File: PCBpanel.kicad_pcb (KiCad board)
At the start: 2 copper layers, 29 x 40 mm, 87 parts, among them P1 CONN_01X05, P1 CONN_01X13, P1 CONN_buzz, P2 CONN_01X03, P2 CONN_01X09, P3 CONN_01X04, P3 CONN_01X09, P3 CONN_01X13, P4 CONN_01X02, Q1 BSS138, Q1 BSS84, Q1 NPN, Q2 BSS138, SW1 SW_PUSH, U1 ESP-12E, U1 GY-NEO6MV2, U2 AP1117, U3 ESP8266_THING, U4 MPU6050, U5 NVSRAM, U6 BMP180, U7 HTU21D

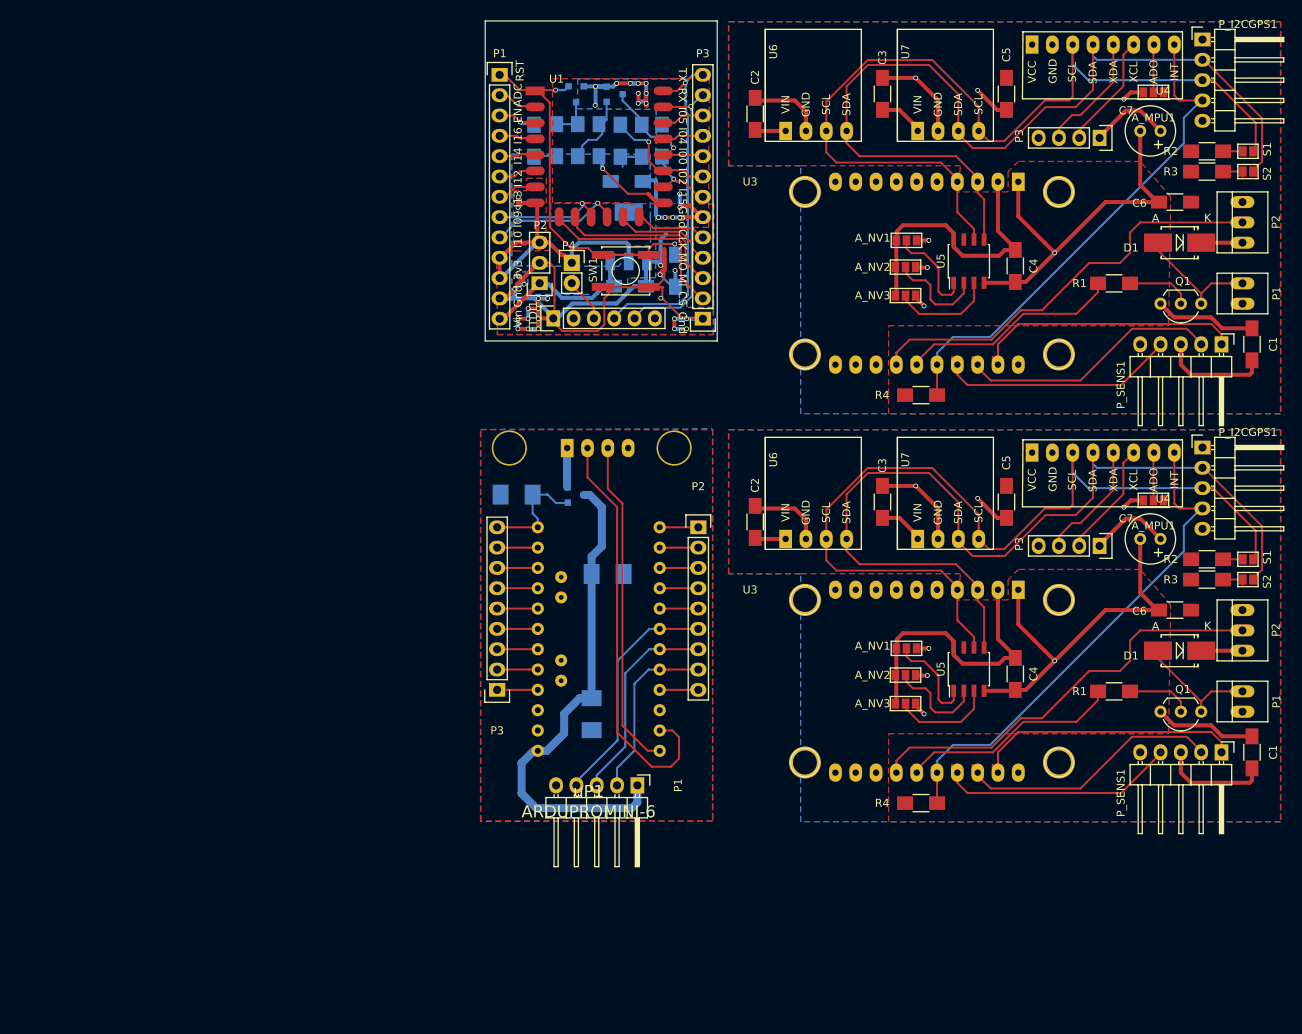
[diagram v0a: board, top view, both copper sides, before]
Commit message: added mounting hole and fixed footprint error
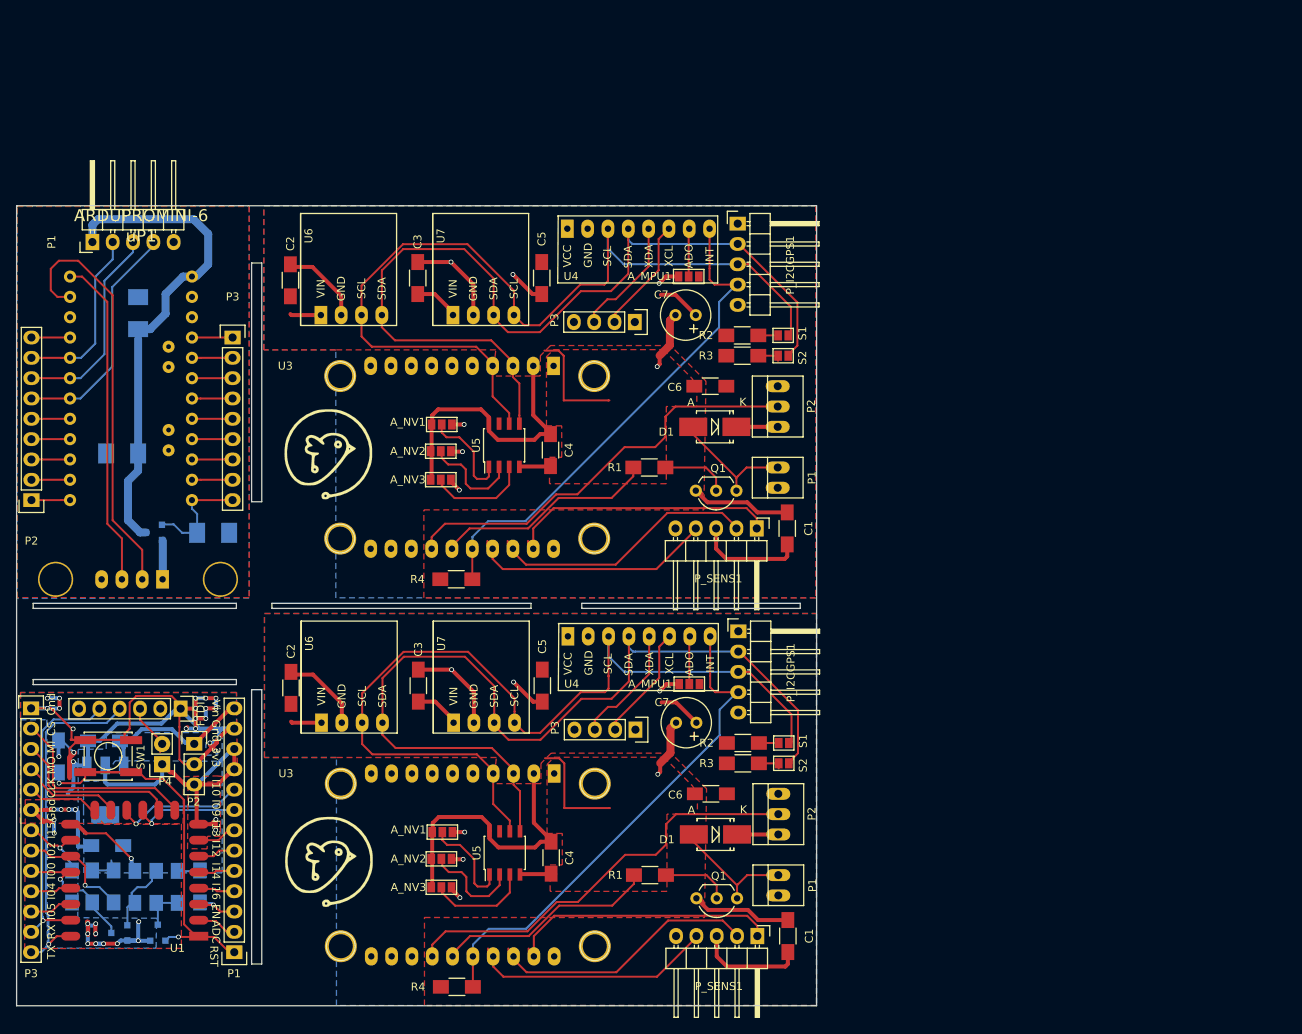
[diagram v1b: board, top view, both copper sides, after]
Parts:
- removed the A_MPU1 at (192.1, 35.8)
- removed the A_MPU1 at (192.1, 86.8)
- removed the A_NV1 at (161.2, 54.3)
- removed the A_NV1 at (161.2, 105.3)
- removed the A_NV2 at (161.1, 57.7)
- removed the A_NV2 at (161.1, 108.7)
- removed the A_NV3 at (161.1, 61.2)
- removed the A_NV3 at (161.1, 112.2)
- removed the C1 at (204.4, 67.3)
- removed the C1 at (204.4, 118.3)
- removed the C2 at (142.3, 38.5)
- removed the C2 at (142.3, 89.5)
- removed the C3 at (158.2, 36.0)
- removed the C3 at (158.2, 87.0)
- removed the C4 at (174.8, 57.5)
- removed the C4 at (174.8, 108.5)
- removed the C5 at (173.7, 36.0)
- removed the C5 at (173.7, 87.0)
- removed the C6 at (194.8, 49.5)
- removed the C6 at (194.8, 100.5)
- removed the C7 at (193.0, 40.6)
- removed the C7 at (193.0, 91.7)
- removed the D1 at (195.4, 54.6)
- removed the D1 at (195.4, 105.6)
- removed the P1 at (203.2, 61.0)
- removed the P1 at (203.2, 112.0)
- removed the P2 at (203.2, 52.1)
- removed the P2 at (203.2, 103.1)
- removed the P3 at (185.4, 41.5)
- removed the P3 at (185.4, 92.5)
- removed the P_I2CGPS1 at (198.2, 29.2)
- removed the P_I2CGPS1 at (198.2, 80.2)
- removed the P_SENS1 at (200.6, 67.3)
- removed the P_SENS1 at (200.6, 118.3)
- removed the Q1 at (198.1, 62.2)
- removed the Q1 at (198.1, 113.2)
- removed the R1 at (187.2, 59.7)
- removed the R1 at (187.2, 110.7)
- removed the R2 at (198.8, 43.2)
- removed the R2 at (198.8, 94.2)
- removed the R3 at (198.8, 45.7)
- removed the R3 at (198.8, 96.7)
- removed the R4 at (163.1, 73.7)
- removed the R4 at (163.1, 124.7)
- removed the S1 at (203.9, 43.2)
- removed the S1 at (203.9, 94.2)
- removed the S2 at (203.9, 45.7)
- removed the S2 at (203.9, 96.7)
- removed the U3 at (191.7, 45.7)
- removed the U3 at (191.7, 96.7)
- removed the U4 at (195.7, 31.6)
- removed the U4 at (195.7, 82.6)
- removed the U5 at (169.0, 56.9)
- removed the U5 at (169.0, 107.9)
- removed the U6 at (143.6, 41.9)
- removed the U6 at (143.6, 92.9)
- removed the U7 at (160.1, 41.9)
- removed the U7 at (160.1, 92.9)
- added A_MPU1: GS_A0, Connect:GS3, F.Cu at (134.0, 58.8)
- added A_MPU1: GS_A0, Connect:GS3, F.Cu at (134.1, 109.8)
- added A_NV1: GS_A0, Connect:GS3, F.Cu at (103.1, 77.3)
- added A_NV1: GS_A0, Connect:GS3, F.Cu at (103.2, 128.3)
- added A_NV2: GS_A1, Connect:GS3, F.Cu at (103.0, 80.7)
- added A_NV2: GS_A1, Connect:GS3, F.Cu at (103.1, 131.6)
- added A_NV3: GS_A2, Connect:GS3, F.Cu at (103.0, 84.2)
- added A_NV3: GS_A2, Connect:GS3, F.Cu at (103.1, 135.2)
- added C1: C, Capacitors_SMD:C_1206_HandSoldering, F.Cu at (146.3, 90.3)
- added C1: C, Capacitors_SMD:C_1206_HandSoldering, F.Cu at (146.4, 141.3)
- added C2: C, Capacitors_SMD:C_1206_HandSoldering, F.Cu at (84.2, 59.3)
- added C2: C, Capacitors_SMD:C_1206_HandSoldering, F.Cu at (84.3, 110.3)
- added C3: C, Capacitors_SMD:C_1206_HandSoldering, F.Cu at (100.1, 59.0)
- added C3: C, Capacitors_SMD:C_1206_HandSoldering, F.Cu at (100.2, 110.0)
- added C4: C, Capacitors_SMD:C_1206_HandSoldering, F.Cu at (116.7, 80.5)
- added C4: C, Capacitors_SMD:C_1206_HandSoldering, F.Cu at (116.8, 131.5)
- added C5: C, Capacitors_SMD:C_1206_HandSoldering, F.Cu at (115.6, 59.0)
- added C5: C, Capacitors_SMD:C_1206_HandSoldering, F.Cu at (115.7, 110.0)
- added C6: C, Capacitors_SMD:C_1206_HandSoldering, F.Cu at (136.7, 72.6)
- added C6: C, Capacitors_SMD:C_1206_HandSoldering, F.Cu at (136.8, 123.5)
- added C7: CP, Capacitors_Elko_ThroughHole:Elko_vert_11.2x6.3mm_RM2.5, F.Cu at (134.9, 63.7)
- added C7: CP, Capacitors_Elko_ThroughHole:Elko_vert_11.2x6.3mm_RM2.5, F.Cu at (135.0, 114.6)
- added D1: DIODE, Diodes_SMD:SMB_Handsoldering, F.Cu at (137.3, 77.6)
- added D1: DIODE, Diodes_SMD:SMB_Handsoldering, F.Cu at (137.4, 128.6)
- added G***: LOGO, Adem_Kicad_logos:adem_logo, F.Cu at (88.9, 81.0)
- added G***: LOGO, Adem_Kicad_logos:adem_logo-txt_17_B_silk, F.Cu at (113.9, 81.8)
- added G***: LOGO, Adem_Kicad_logos:adem_logo, F.Cu at (89.0, 132.0)
- added G***: LOGO, Adem_Kicad_logos:adem_logo-txt_17_B_silk, F.Cu at (114.0, 132.8)
- added P1: CONN_buzz, Connect:PINHEAD1-2, F.Cu at (145.1, 84.0)
- added P1: CONN_buzz, Connect:PINHEAD1-2, F.Cu at (145.2, 134.9)
- added P2: CONN_01X03, Connect:PINHEAD1-3, F.Cu at (145.1, 75.1)
- added P2: CONN_01X03, Connect:PINHEAD1-3, F.Cu at (145.2, 126.0)
- added P3: CONN_01X04, Pin_Headers:Pin_Header_Straight_1x04, F.Cu at (127.3, 64.5)
- added P3: CONN_01X04, Pin_Headers:Pin_Header_Straight_1x04, F.Cu at (127.4, 115.5)
- added P_I2CGPS1: CONN_01X05, Pin_Headers:Pin_Header_Angled_1x05, F.Cu at (140.1, 52.2)
- added P_I2CGPS1: CONN_01X05, Pin_Headers:Pin_Header_Angled_1x05, F.Cu at (140.2, 103.2)
- added P_SENS1: CONN_01X05, Pin_Headers:Pin_Header_Angled_1x05, F.Cu at (142.5, 90.3)
- added P_SENS1: CONN_01X05, Pin_Headers:Pin_Header_Angled_1x05, F.Cu at (142.6, 141.3)
- added Q1: NPN, TO_SOT_Packages_THT:TO-92_Inline_Wide, F.Cu at (140.0, 85.6)
- added Q1: NPN, TO_SOT_Packages_THT:TO-92_Inline_Wide, F.Cu at (140.1, 136.6)
- added R1: R, Resistors_SMD:R_1206_HandSoldering, F.Cu at (129.1, 82.7)
- added R1: R, Resistors_SMD:R_1206_HandSoldering, F.Cu at (129.2, 133.7)
- added R2: R, Resistors_SMD:R_1206_HandSoldering, F.Cu at (140.7, 66.2)
- added R2: R, Resistors_SMD:R_1206_HandSoldering, F.Cu at (140.8, 117.2)
- added R3: R, Resistors_SMD:R_1206_HandSoldering, F.Cu at (140.7, 68.7)
- added R3: R, Resistors_SMD:R_1206_HandSoldering, F.Cu at (140.8, 119.7)
- added R4: R, Resistors_SMD:R_1206_HandSoldering, F.Cu at (105.0, 96.7)
- added R4: R, Resistors_SMD:R_1206_HandSoldering, F.Cu at (105.0, 147.6)
- added S1: GS1, Connect:GS2, F.Cu at (145.8, 66.2)
- added S1: GS1, Connect:GS2, F.Cu at (145.9, 117.2)
- added S2: S2, Connect:GS2, F.Cu at (145.8, 68.7)
- added S2: S2, Connect:GS2, F.Cu at (145.9, 119.7)
- added U3: ESP8266_THING, ADEM:ESP8266_THING, F.Cu at (133.6, 68.7)
- added U3: ESP8266_THING, ADEM:ESP8266_THING, F.Cu at (133.7, 119.7)
- added U4: MPU6050, ADEM:MPU6050_angled, F.Cu at (137.6, 54.6)
- added U4: MPU6050, ADEM:MPU6050_angled, F.Cu at (137.7, 105.5)
- added U5: NVSRAM, Housings_SOIC:SOIC-8_3.9x4.9mm_Pitch1.27mm, F.Cu at (110.9, 79.9)
- added U5: NVSRAM, Housings_SOIC:SOIC-8_3.9x4.9mm_Pitch1.27mm, F.Cu at (111.0, 130.9)
- added U6: BMP180, ADEM:BMP180, F.Cu at (85.5, 64.9)
- added U6: BMP180, ADEM:BMP180, F.Cu at (85.6, 115.9)
- added U7: HTU21D, ADEM:HTU21D, F.Cu at (102.0, 64.9)
- added U7: HTU21D, ADEM:HTU21D, F.Cu at (102.1, 115.9)
- moved Q2 121.8 mm to (62.8, 140.9), turned to 270 degrees
- moved R6 118.9 mm to (56.9, 135.1), turned to 270 degrees
- moved Q1 117.1 mm to (67.7, 140.9), turned to 180 degrees
- moved R3 115.8 mm to (59.5, 135.1), turned to 270 degrees
- moved P1 114.6 mm to (77.2, 143.3), turned to 180 degrees
- moved U1 113.7 mm to (72.8, 141.3), turned to 180 degrees
- moved R4 112.7 mm to (62.1, 135.1), turned to 270 degrees
- moved C2 109.9 mm to (64.8, 135.1), turned to 90 degrees
- moved R2 107.2 mm to (67.5, 135.1), turned to 270 degrees
- moved uP1 106.7 mm to (54.1, 52.5), turned to 0 degrees
- moved C4 105.4 mm to (61.3, 130.0), turned to 180 degrees
- moved R1 104.7 mm to (70.1, 135.1), turned to 270 degrees
- moved R5 102.1 mm to (72.9, 135.1), turned to 270 degrees
- moved C1 98.1 mm to (55.2, 118.8), turned to 90 degrees
- moved P3 97.1 mm to (51.8, 112.8), turned to 0 degrees
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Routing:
- net GND: track 358.0 -> 292.0 mm
- net (no net): track 100.0 -> 128.0 mm
- net VCC: track 215.3 -> 206.1 mm
- net Net-(Q1-Pad2): track 21.9 -> 22.6 mm
- net Net-(D1-Pad2): track 31.1 -> 31.8 mm
- net SDA: track 251.7 -> 251.2 mm
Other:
- board size 29 x 40 mm -> 100 x 100 mm
- board text added: "github.com/timelab/ADEM-hardware github.com/timelab/ADEM www.ik-adem.be"
